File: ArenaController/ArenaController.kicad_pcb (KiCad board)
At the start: 2 copper layers, 86.6 x 104.5 mm, 45 parts, among them J1 RJ45, J2 RJ45, J3 5Pin_5mm_plus_2.54_pin, J4 RJ45, J5 RJ45, J6 RJ45, J7 Barrel_Jack, Q1 IRLIZ44N, Q2 IRLIZ44N, Q3 IRLIZ44N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

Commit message: Update to shit.
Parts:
- removed D1, D2: rLED, LED_THT:LED_D10.0mm
- removed D3: gLED, LED_THT:LED_D10.0mm
- removed D4: yLED, LED_THT:LED_D10.0mm
- removed D5: LED, LED_THT:LED_D10.0mm
- removed H3, H4: MountingHole, MountingHole:MountingHole_3.2mm_M3
- removed J3: 5Pin_5mm_plus_2.54_pin, footprints:5pin_5mmpitch_plus_2.54_combo
- removed J7: Barrel_Jack, Connector_BarrelJack:BarrelJack_Horizontal
- removed Q5: IRLIZ44N, Package_TO_SOT_THT:TO-220F-3_Vertical
- removed R1, R10, R11, R12, R13, R7, R8, R9: 10k, Resistor_THT:R_Axial_DIN0207_L6.3mm_D2.5mm_P10.16mm_Horizontal
- removed R2, R3, R4, R5, R6: 330, Resistor_THT:R_Axial_DIN0207_L6.3mm_D2.5mm_P10.16mm_Horizontal
- removed U1: ESP32-DEVKIT-V1, ESP32DK1:MODULE_ESP32_DEVKIT_V1
- removed U2: 20mmx50mm_buckboost, footprints:buckboost_mount
- removed kibuzzard-63898CDD: G***, kibuzzard-63898CDD
- removed kibuzzard-638A2249, kibuzzard-638A2249123: G***, kibuzzard-638A2249
- removed kibuzzard-638A2274: G***, kibuzzard-638A2274
- Q1, Q2, Q3, Q4: footprint Package_TO_SOT_THT:TO-220F-3_Vertical -> Package_TO_SOT_THT:TO-220F-3_Horizontal_TabDown
- moved H1 46.2 mm to (48.3, 48.3)
- moved J4 43.2 mm to (129.7, 99.3)
- moved J5 43.2 mm to (129.7, 118.4)
- moved J6 43.2 mm to (129.7, 77.6)
- moved kibuzzard-638A2165 43.2 mm to (128.3, 126.5)
- moved kibuzzard-638A2178 43.2 mm to (128.1, 85.1)
- moved H2 43.2 mm to (48.8, 142.6)
- moved J1 43.2 mm to (43.4, 108.1)
- moved J2 43.2 mm to (43.4, 92.6)
- moved kibuzzard-638A2138 43.2 mm to (46.7, 85.1)
- moved kibuzzard-638A214B 43.2 mm to (46.7, 100.5)
- moved kibuzzard-638A219C 43.2 mm to (126.9, 106.9)
- moved Q2 31.5 mm to (153.8, 101.6)
- moved Q1 30.0 mm to (151.0, 66.0)
- moved Q4 17.6 mm to (144.8, 115.4)
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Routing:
- net +5V: track 132.6 -> 0.00 mm, vias 2 -> 0
- net Net-(D5-A): track 116.7 -> 0.00 mm
- net +3V3: track 110.0 -> 0.00 mm
- net /s_Yellow: track 82.2 -> 0.00 mm
- net /T_A_End: track 78.4 -> 0.00 mm, vias 1 -> 0
- net /s_Horn: track 69.7 -> 0.00 mm
- net /T_A_Start: track 68.3 -> 0.00 mm
- net +12V: track 64.7 -> 0.00 mm
- net Net-(D3-A): track 58.4 -> 0.00 mm, vias 1 -> 0
- net /s_Green: track 50.4 -> 0.00 mm
- net /Dis_Serial_Tx: track 48.2 -> 0.00 mm
- net /Dis_serial_Rx: track 46.9 -> 0.00 mm
- net Net-(D2-Pad2): track 46.0 -> 0.00 mm, vias 1 -> 0
- net Net-(D4-A): track 43.3 -> 0.00 mm
- net /s_Red_2: track 37.4 -> 0.00 mm, vias 1 -> 0
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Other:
- board size 86.6 x 104.5 mm -> 86.7 x 104.5 mm

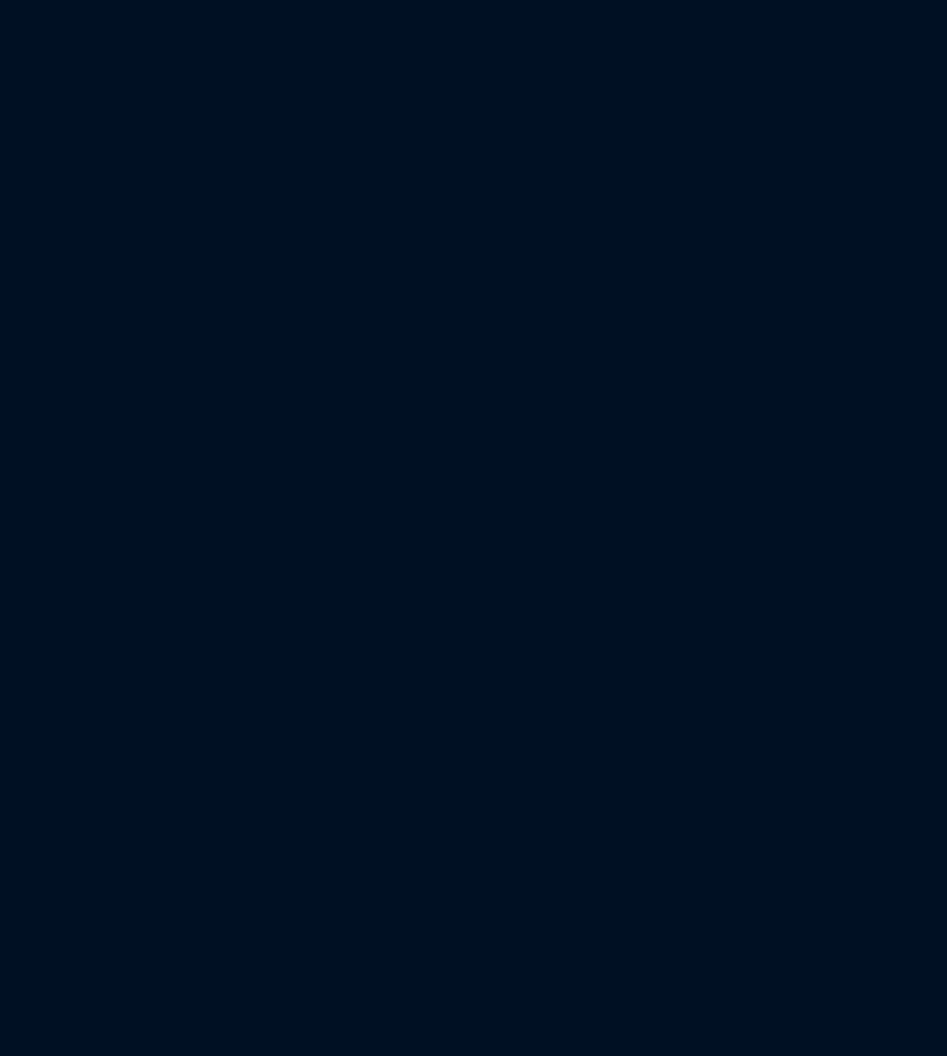
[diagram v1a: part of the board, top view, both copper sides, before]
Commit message: Add microswitch for start buttons.
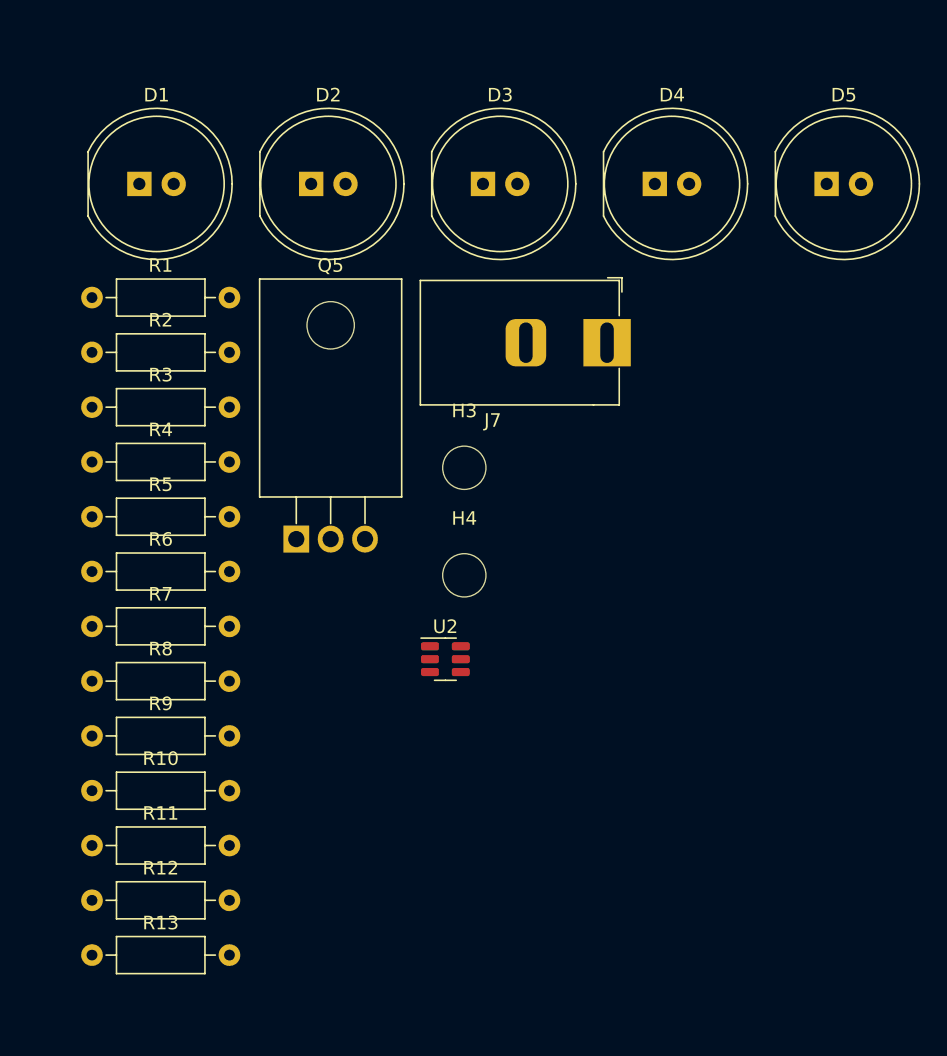
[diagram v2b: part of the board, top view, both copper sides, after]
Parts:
- added D1: rLED, LED_THT:LED_D10.0mm, F.Cu at (194.7, 66.8)
- added D2: rLED, LED_THT:LED_D10.0mm, F.Cu at (207.4, 66.8)
- added D3: gLED, LED_THT:LED_D10.0mm, F.Cu at (220.1, 66.8)
- added D4: yLED, LED_THT:LED_D10.0mm, F.Cu at (232.8, 66.8)
- added D5: LED, LED_THT:LED_D10.0mm, F.Cu at (245.5, 66.8)
- added H3: MountingHole, MountingHole:MountingHole_3.2mm_M3, F.Cu at (218.7, 87.8)
- added H4: MountingHole, MountingHole:MountingHole_3.2mm_M3, F.Cu at (218.7, 95.7)
- added J7: Barrel_Jack, footprints:BarrelJack_Horizontal_TwoPin, F.Cu at (229.3, 78.5)
- added Q5: IRLIZ44N, Package_TO_SOT_THT:TO-220F-3_Horizontal_TabDown, F.Cu at (206.3, 93.0)
- added R1: 10k, Resistor_THT:R_Axial_DIN0207_L6.3mm_D2.5mm_P10.16mm_Horizontal, F.Cu at (191.2, 75.2)
- added R10: 10k, Resistor_THT:R_Axial_DIN0207_L6.3mm_D2.5mm_P10.16mm_Horizontal, F.Cu at (191.2, 111.6)
- added R11: 10k, Resistor_THT:R_Axial_DIN0207_L6.3mm_D2.5mm_P10.16mm_Horizontal, F.Cu at (191.2, 115.7)
- added R12: 10k, Resistor_THT:R_Axial_DIN0207_L6.3mm_D2.5mm_P10.16mm_Horizontal, F.Cu at (191.2, 119.7)
- added R13: 10k, Resistor_THT:R_Axial_DIN0207_L6.3mm_D2.5mm_P10.16mm_Horizontal, F.Cu at (191.2, 123.8)
- added R2: 330, Resistor_THT:R_Axial_DIN0207_L6.3mm_D2.5mm_P10.16mm_Horizontal, F.Cu at (191.2, 79.2)
- added R3: 330, Resistor_THT:R_Axial_DIN0207_L6.3mm_D2.5mm_P10.16mm_Horizontal, F.Cu at (191.2, 83.3)
- added R4: 330, Resistor_THT:R_Axial_DIN0207_L6.3mm_D2.5mm_P10.16mm_Horizontal, F.Cu at (191.2, 87.3)
- added R5: 330, Resistor_THT:R_Axial_DIN0207_L6.3mm_D2.5mm_P10.16mm_Horizontal, F.Cu at (191.2, 91.4)
- added R6: 330, Resistor_THT:R_Axial_DIN0207_L6.3mm_D2.5mm_P10.16mm_Horizontal, F.Cu at (191.2, 95.4)
- added R7: 10k, Resistor_THT:R_Axial_DIN0207_L6.3mm_D2.5mm_P10.16mm_Horizontal, F.Cu at (191.2, 99.5)
- added R8: 10k, Resistor_THT:R_Axial_DIN0207_L6.3mm_D2.5mm_P10.16mm_Horizontal, F.Cu at (191.2, 103.5)
- added R9: 10k, Resistor_THT:R_Axial_DIN0207_L6.3mm_D2.5mm_P10.16mm_Horizontal, F.Cu at (191.2, 107.6)
- added U2: TPS563200, Package_TO_SOT_SMD:SOT-23-6, F.Cu at (217.3, 101.9)

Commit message: Added new files, swap to new FET for toggling, added FET as symbols.
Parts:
- removed D1, D2: rLED, LED_THT:LED_D10.0mm
- removed D3: gLED, LED_THT:LED_D10.0mm
- removed D4: yLED, LED_THT:LED_D10.0mm
- removed D5: LED, LED_THT:LED_D10.0mm
- removed R1, R10, R11, R12, R13, R7, R8, R9: 10k, Resistor_THT:R_Axial_DIN0207_L6.3mm_D2.5mm_P10.16mm_Horizontal
- removed U2: TPS563200, Package_TO_SOT_SMD:SOT-23-6
- added J8: Screw_Terminal_01x04, TerminalBlock_MetzConnect:TerminalBlock_MetzConnect_Type011_RT05504HBWC_1x04_P5.00mm_Horizontal, F.Cu at (95.5, 140.2)
- added PS1: ~, Package_TO_SOT_SMD:TSOT-23-6_HandSoldering, F.Cu at (190.3, 45.3)
- added R16: 10k, Resistor_THT:R_Axial_DIN0207_L6.3mm_D2.5mm_P10.16mm_Horizontal, F.Cu at (175.1, 45.1)
- added R17: 10k, Resistor_THT:R_Axial_DIN0207_L6.3mm_D2.5mm_P10.16mm_Horizontal, F.Cu at (175.1, 49.1)
- Q1, Q2, Q3, Q4: value IRLIZ44N -> FS3400; footprint Package_TO_SOT_THT:TO-220F-3_Horizontal_TabDown -> Package_TO_SOT_SMD:SOT-23; moved to F.Cu
- Q5: value IRLIZ44N -> FS3400; footprint Package_TO_SOT_THT:TO-220F-3_Horizontal_TabDown -> Package_TO_SOT_SMD:SOT-23
- moved J7 169.4 mm to (60.9, 59.8), turned to -90 degrees
- moved H4 130.5 mm to (100.0, 150.0)
- moved H3 124.6 mm to (100.0, 50.0)
- moved H2 7.46 mm to (50.0, 150.0)
- moved H1 2.46 mm to (50.0, 50.0)
- turned Q4 to 180 degrees
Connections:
- J4 pad 1: +3V3 -> unconnected-(J4-Pad1)
- J4 pad 2: /G_Start -> unconnected-(J4-Pad2)
- J4 pad 3: /G_Pause -> unconnected-(J4-Pad3)
- J4 pad 4: /G_End -> /G_Start
- J4 pad 5: /G_Reset -> /G_Pause
- J4 pad 6: unconnected-(J4-Pad6) -> /G_End
- J4 pad 7: unconnected-(J4-Pad7) -> /G_Reset
- J4 pad 8: unconnected-(J4-Pad8) -> GND
- J5 pad 8: +3V3 -> GND
- J6 pad 8: +3V3 -> GND
- Q1 pad 2: /s_Green -> GND
- Q1 pad 3: GND -> /s_Green
- Q2 pad 2: /s_Red_1 -> GND
- Q2 pad 3: GND -> /s_Red_1
- Q3 pad 2: /s_Horn -> GND
- Q3 pad 3: GND -> /s_Horn
- Q4 pad 2: /s_Yellow -> GND
- Q4 pad 3: GND -> /s_Yellow
- Q5 pad 2: /s_Red_2 -> GND
- Q5 pad 3: GND -> /s_Red_2
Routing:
- removed copper zone on B.Cu, net GND
- removed copper zone on F.Cu, net GND
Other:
- board size 86.7 x 104.5 mm -> 3.2 x 14.7 mm

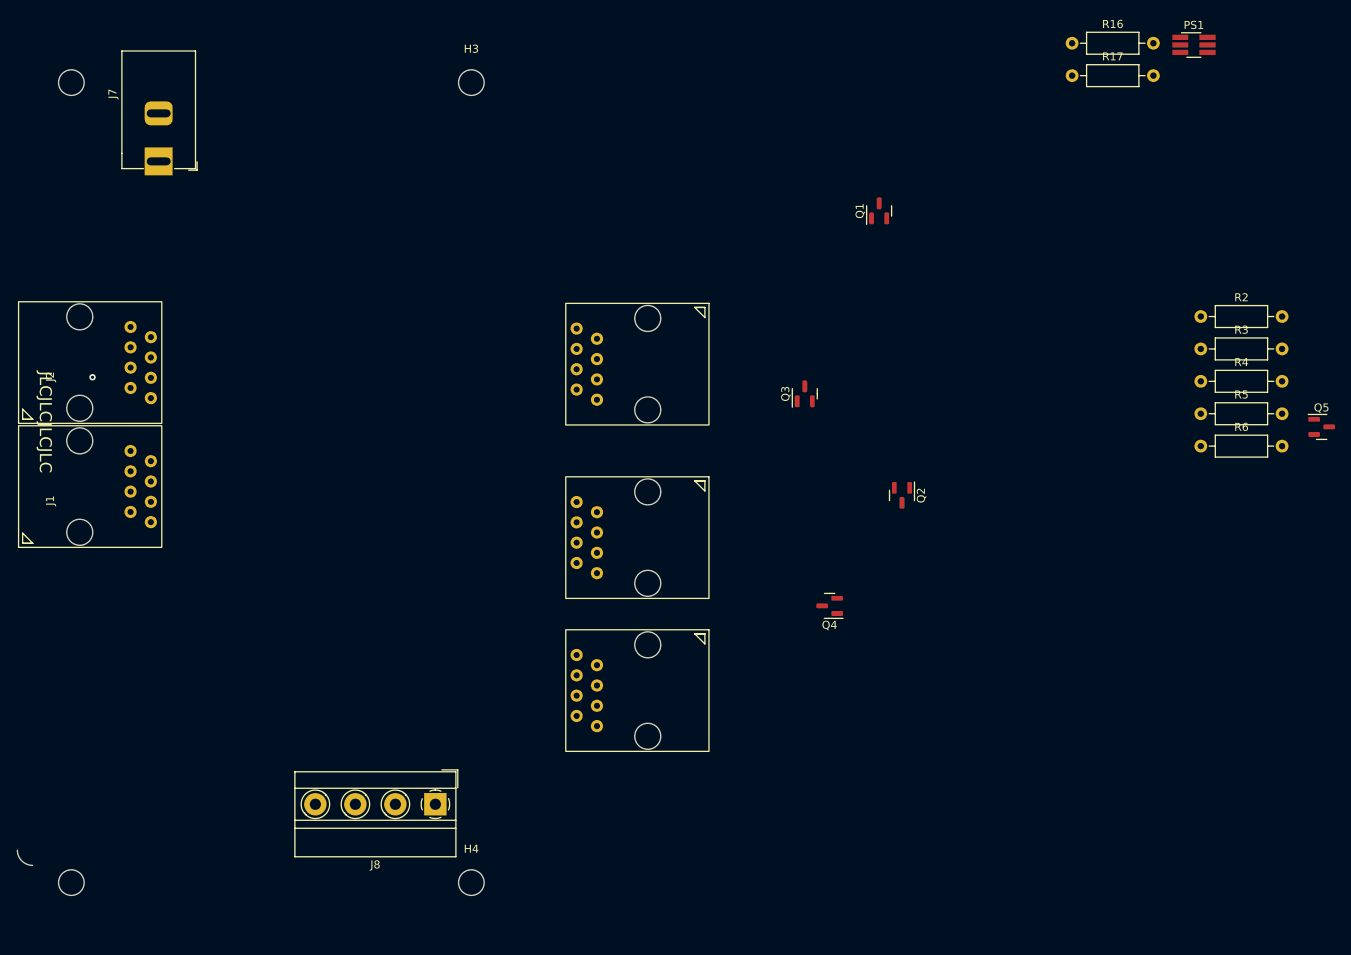
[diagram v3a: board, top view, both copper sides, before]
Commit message: Added new DC DC symbol.
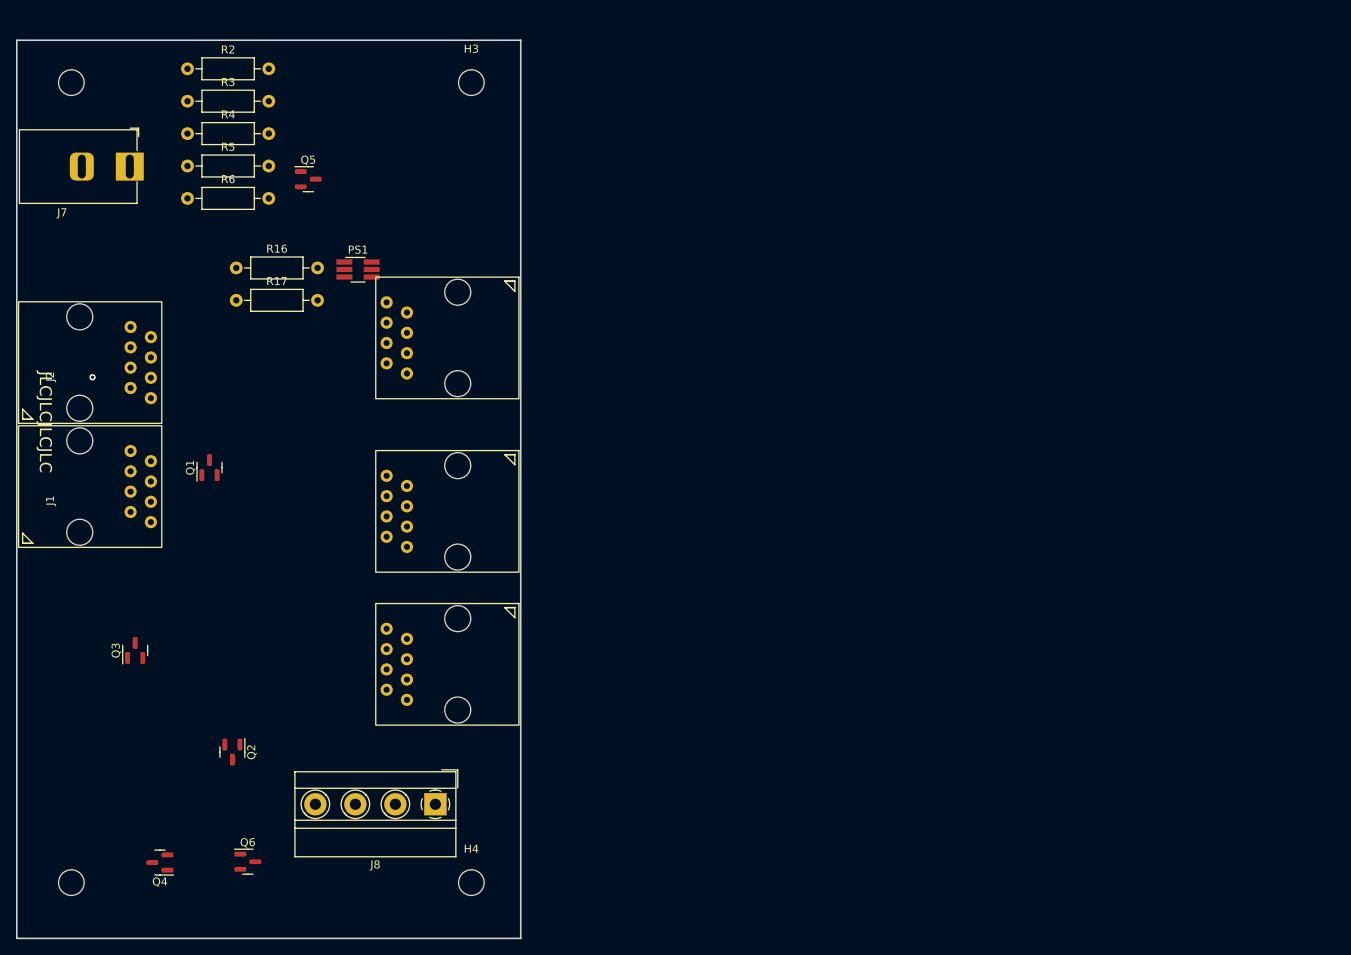
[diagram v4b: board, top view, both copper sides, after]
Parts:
- added Q6: Q_NMOS_GSD, Package_TO_SOT_SMD:SOT-23, F.Cu at (72.1, 147.4)
- moved Q5 130.4 mm to (79.6, 62.1)
- moved R2 130.4 mm to (64.5, 48.3)
- moved R3 130.4 mm to (64.5, 52.3)
- moved R4 130.4 mm to (64.5, 56.4)
- moved R5 130.4 mm to (64.5, 60.4)
- moved R6 130.4 mm to (64.5, 64.5)
- moved PS1 108.2 mm to (85.8, 73.4)
- moved R16 108.2 mm to (70.6, 73.2)
- moved R17 108.2 mm to (70.6, 77.2)
- moved Q2 89.6 mm to (70.1, 133.7)
- moved Q1 89.6 mm to (67.3, 98.1)
- moved Q3 89.6 mm to (58.0, 121.0)
- moved Q4 89.6 mm to (61.1, 147.5)
- moved J4 24.0 mm to (105.9, 96.0)
- moved J5 24.0 mm to (105.9, 115.1)
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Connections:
- J5 pad 4: unconnected-(J5-Pad4) -> /T_B_End
- J5 pad 5: /T_B_End -> unconnected-(J5-Pad5)
- J6 pad 4: unconnected-(J6-Pad4) -> /T_A_Start
- J6 pad 5: /T_A_Start -> unconnected-(J6-Pad5)
- R16 pad 1: /status_LED -> +3.3V
- R16 pad 2: GND -> /status_LED
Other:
- board size 3.2 x 14.7 mm -> 63 x 112.3 mm
